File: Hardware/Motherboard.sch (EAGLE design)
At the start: 66 parts, among them J1 MICROMOD-2222-C, J10 MICRO-SD-PUSH-PUSH-EXT-PIN, J2 Vertical Qwiic Connector, J4 QWIIC_RIGHT_ANGLE, J5 CORTEX_JTAG_DEBUG_MINIMUM_PTH, J6 MICROMOD_CARRIER, J7 MICROMOD_CARRIER, Q1 3.1A/30V/105mΩ, U2 MCP73831, U5 AP7361C-33

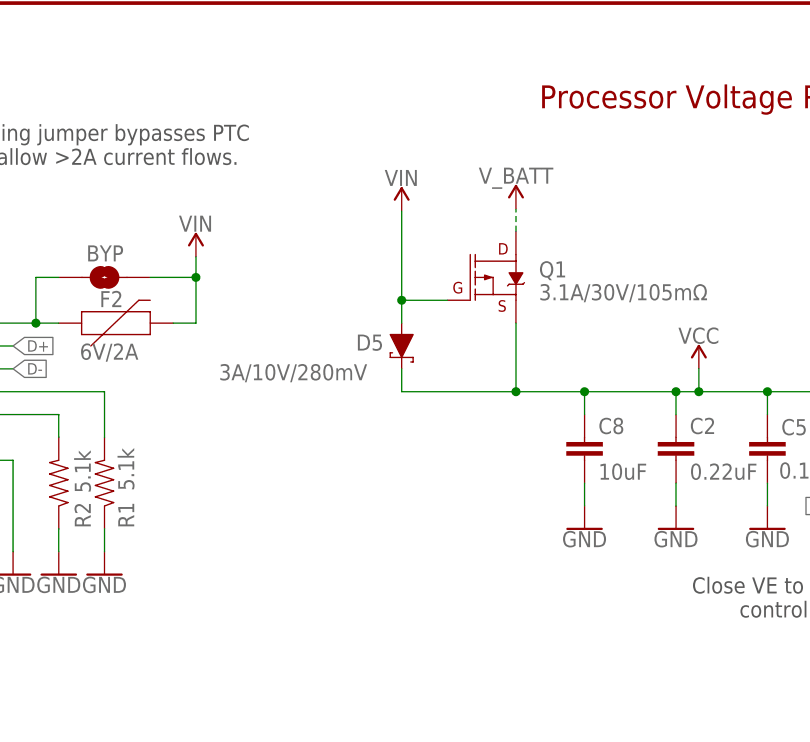
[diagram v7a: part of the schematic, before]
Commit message: Adds 10k pull down to PCHAN MOSFET
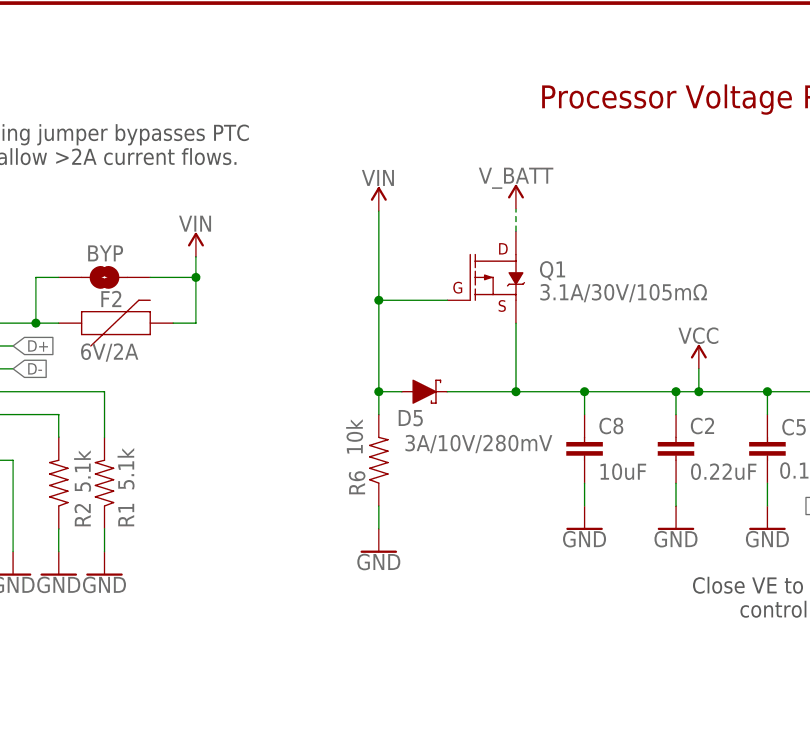
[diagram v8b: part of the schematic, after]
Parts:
- added R6: 10k, SparkFun-Resistors:10KOHM-0603-1/10W-1%
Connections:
- net GND: now also R6.1
- net VIN: now also R6.2
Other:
- moved on the sheet: D5
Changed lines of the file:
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@@
 <part name="Q1" library="SparkFun-DiscreteSemi" deviceset="MOSFET_PCH" device="-DMG2307L" value="3.1A/30V/105mΩ"/>
 <part name="GND6" library="SparkFun-PowerSymbols" deviceset="GND" device=""/>
+<part name="R6" library="SparkFun-Resistors" deviceset="10KOHM" device="-0603-1/10W-1%" value="10k"/>
+<part name="GND8" library="SparkFun-PowerSymbols" deviceset="GND" device=""/>
 </parts>
 <sheets>
@@
 <attribute name="VALUE" x="289.56" y="185.674" size="1.778" layer="96" font="vector" rot="MR0" align="bottom-center"/>
 </instance>
-<instance part="D5" gate="G$1" x="266.7" y="241.3" smashed="yes" rot="R270">
-<attribute name="NAME" x="261.62" y="240.792" size="1.778" layer="95" font="vector"/>
-<attribute name="VALUE" x="246.38" y="239.268" size="1.778" layer="96" font="vector" align="top-left"/>
+<instance part="D5" gate="G$1" x="269.24" y="236.22" smashed="yes">
+<attribute name="NAME" x="269.24" y="234.188" size="1.778" layer="95" font="vector" rot="R180"/>
+<attribute name="VALUE" x="266.954" y="231.394" size="1.778" layer="96" font="vector" align="top-left"/>
 </instance>
 <instance part="5V_LED" gate="G$1" x="227.076" y="22.606" smashed="yes" rot="R90">
@@
 <attribute name="VALUE" x="227.076" y="12.192" size="1.778" layer="96" font="vector" align="top-center"/>
 </instance>
-<instance part="SUPPLY13" gate="G$1" x="266.7" y="256.286" smashed="yes">
-<attribute name="VALUE" x="266.7" y="259.08" size="1.778" layer="96" align="bottom-center"/>
+<instance part="SUPPLY13" gate="G$1" x="264.16" y="256.286" smashed="yes">
+<attribute name="VALUE" x="264.16" y="259.08" size="1.778" layer="96" align="bottom-center"/>
 </instance>
 <instance part="SUPPLY24" gate="G$1" x="227.076" y="53.34" smashed="yes">
@@
 <instance part="GND6" gate="1" x="177.8" y="139.7" smashed="yes">
 <attribute name="VALUE" x="177.8" y="139.446" size="1.778" layer="96" font="vector" align="top-center"/>
+</instance>
+<instance part="R6" gate="G$1" x="264.16" y="228.6" smashed="yes" rot="R90">
+<attribute name="NAME" x="262.636" y="226.06" size="1.778" layer="95" font="vector" rot="R90" align="bottom-center"/>
+<attribute name="VALUE" x="260.604" y="231.14" size="1.778" layer="96" font="vector" rot="R90" align="top-center"/>
+</instance>
+<instance part="GND8" gate="1" x="264.16" y="218.44" smashed="yes">
+<attribute name="VALUE" x="264.16" y="218.186" size="1.778" layer="96" font="vector" align="top-center"/>
 </instance>
 </instances>
@@
 <junction x="345.44" y="142.24"/>
 </segment>
+<segment>
+<pinref part="GND8" gate="1" pin="GND"/>
+<pinref part="R6" gate="G$1" pin="1"/>
+<wire x1="264.16" y1="220.98" x2="264.16" y2="223.52" width="0.1524" layer="91"/>
+</segment>
 </net>
 <net name="PWR_EN0" class="0">
@@
 <pinref part="D5" gate="G$1" pin="A"/>
 <pinref part="SUPPLY13" gate="G$1" pin="VIN"/>
-<wire x1="266.7" y1="243.84" x2="266.7" y2="246.38" width="0.1524" layer="91"/>
 <pinref part="Q1" gate="G$1" pin="G"/>
-<wire x1="266.7" y1="246.38" x2="266.7" y2="256.286" width="0.1524" layer="91"/>
-<wire x1="271.78" y1="246.38" x2="266.7" y2="246.38" width="0.1524" layer="91"/>
-<junction x="266.7" y="246.38"/>
+<wire x1="271.78" y1="246.38" x2="264.16" y2="246.38" width="0.1524" layer="91"/>
+<wire x1="264.16" y1="246.38" x2="264.16" y2="256.286" width="0.1524" layer="91"/>
+<pinref part="R6" gate="G$1" pin="2"/>
+<wire x1="264.16" y1="233.68" x2="264.16" y2="236.22" width="0.1524" layer="91"/>
+<junction x="264.16" y="246.38"/>
+<wire x1="264.16" y1="236.22" x2="264.16" y2="246.38" width="0.1524" layer="91"/>
+<wire x1="264.16" y1="236.22" x2="266.7" y2="236.22" width="0.1524" layer="91"/>
+<junction x="264.16" y="236.22"/>
 </segment>
 <segment>
@@
 <junction x="287.02" y="236.22"/>
 <pinref part="D5" gate="G$1" pin="C"/>
-<wire x1="266.7" y1="238.76" x2="266.7" y2="236.22" width="0.1524" layer="91"/>
-<wire x1="266.7" y1="236.22" x2="279.4" y2="236.22" width="0.1524" layer="91"/>
+<wire x1="271.78" y1="236.22" x2="279.4" y2="236.22" width="0.1524" layer="91"/>
 <junction x="279.4" y="236.22"/>
 </segment>
